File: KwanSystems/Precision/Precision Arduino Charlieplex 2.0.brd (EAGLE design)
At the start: 76.2 x 76.2 mm, 155 parts, among them J001 M04NOSILK2, J002 M04NOSILK2, J003 M06NOSILK, J201 GP-2106, J202 M06NOSILK, J405 M08NOSILK2, J406 M08NOSILK2, U201 1.8V, U202 TXB0104RUT, U401 ATMEGA328, U501 FT232RLSSOP, U602 ZF7, Y401 16MHz

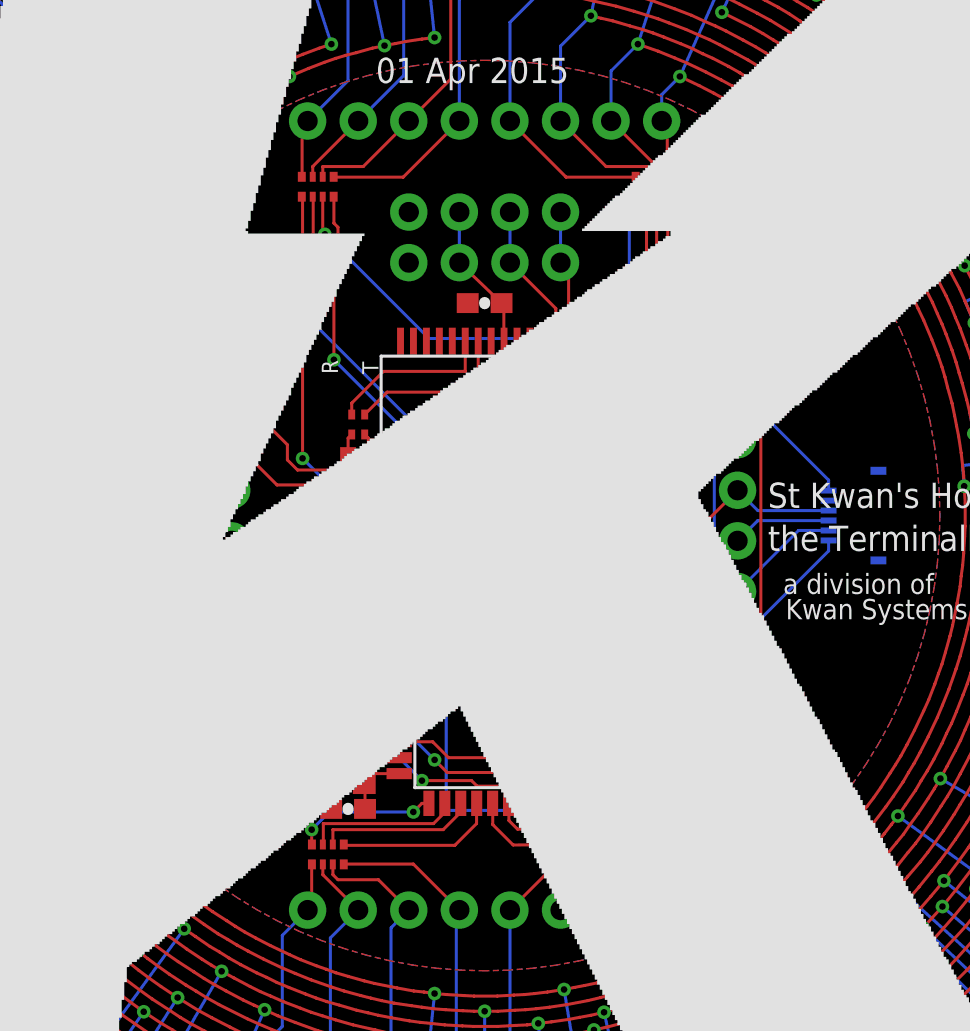
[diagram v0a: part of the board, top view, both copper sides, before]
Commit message: Added Yukari4, changed it over to use templates
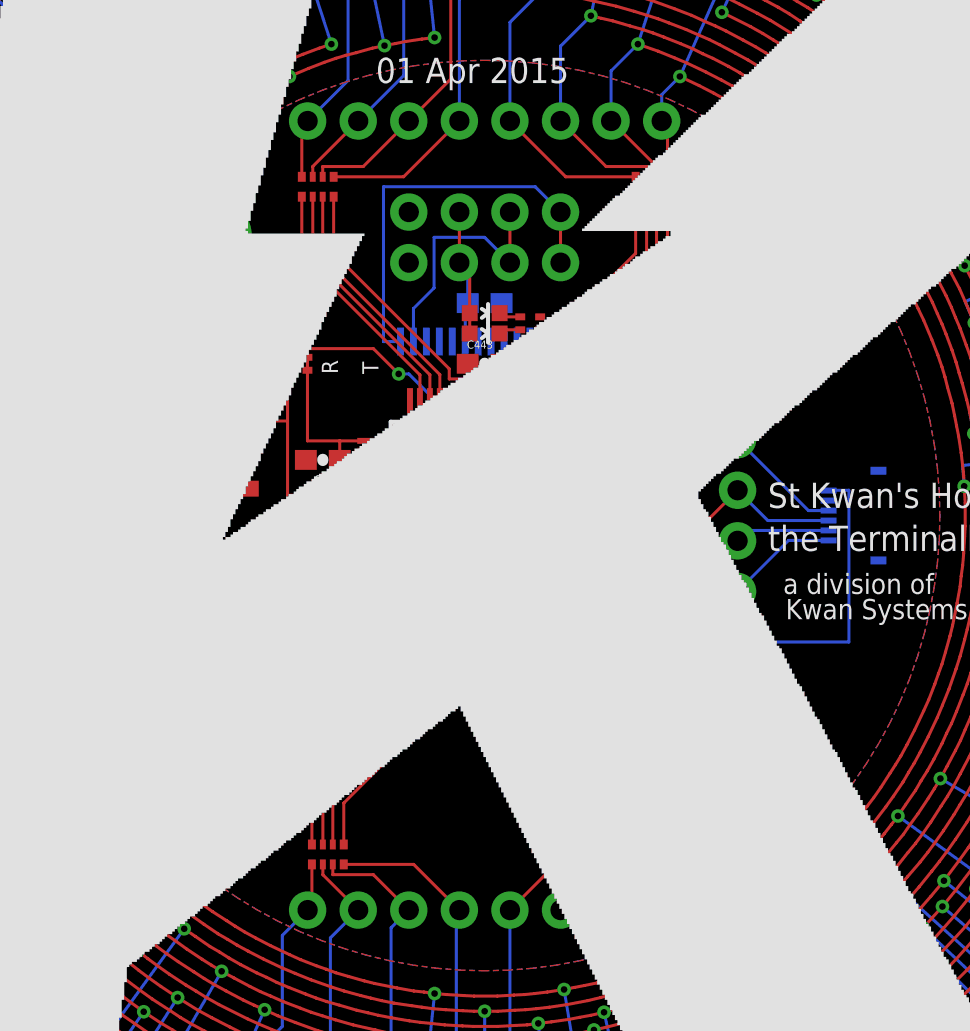
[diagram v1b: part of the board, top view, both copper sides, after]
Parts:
- removed C204: 1uF, SparkFun:0402-CAP
- removed C214: 100nF, SparkFun:0402-CAP
- removed C407, C408: 18pF, SparkFun:0603-CAP
- removed C418: 4.7uF, SparkFun:0603-CAP
- removed C420: 100nF, SparkFun:0603-CAP
- removed J003: M06NOSILK, KwanSystems:M06SIP
- removed U201: 1.8V, KwanSystems:SOT-23-5
- removed U602: ZF7, KwanSystems:SC-70-6
- removed Y401: 16MHz, KwanSystems:CRYSTAL_SMD
- added C201: 1uF, KwanSystems:CKCM25
- added C205, C423, C443, C451: 1uF, SparkFun-Capacitors:0603-CAP
- added C461: 33pF, KwanSystems:CKCM25
- added S458: B3U-1000P, KwanSystems:B3U-1000P
- added U2: AP7312, KwanSystems:SOT-23-6
- added Y1: 12MHz, KwanSystems:CRYSTAL_SMD_2MM_2_5MM
- JP1, JP2, JP3, JP4: value STAND-OFF -> STANDOFF; device SparkFun:STAND-OFF -> KwanSystems:STANDOFF
- U401: value ATMEGA328 -> LPC2148; device SparkFun:TQFP32-08 -> SparkFun:SQFP-S-10X10-64
- moved R606 16.0 mm to (28.7, 45.7), turned to 90 degrees
- moved S429 15.9 mm to (25.9, 41.1), turned to 90 degrees
- moved C215 13.0 mm to (48.0, 33.8), turned to 0 degrees
- moved D501 10.4 mm to (38.1, 48.3), turned to 270 degrees
- moved U401 10.2 mm to (38.1, 38.1)
- moved R500 10.0 mm to (40.4, 47.8), turned to 90 degrees
- moved D502 9.01 mm to (38.1, 47.2), turned to 270 degrees
- moved C502 5.86 mm to (30.0, 38.4)
- flipped C010 to the bottom
- flipped U501 to the bottom
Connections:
- removed net AREF: C420.1, U401.20
- removed net AT_RX: U401.30, U602.4
- removed net AT_TX: U202.9, U401.31, U501.5
- removed net BYP: C214.1, U201.4
- removed net RX_SEL: J003.2, R606.4, U401.16, U602.6
- removed net VCC: C010.1, C204.1, C418.2, D501.A, D502.A, J001.3, J002.3, J003.5, R606.1, R606.2, U201.1, U201.3, U202.11, U401.18, U401.4, U401.6, U501.20, U501.4, U602.5
- new net 3.3V: C201.4, C423.1, C443.1, C451.1, R606.1, R606.2, U2.1, U202.11, U401.23, U401.43, U401.49, U401.51, U401.63, U401.7
- new net 5V: C010.1, C205.1, D501.A, D502.A, J001.3, J002.3, U2.3, U2.4, U2.5, U501.20, U501.4
- new net BSL: R606.3, S458.P$1, U401.41
- new net GPS_RX: U202.9, U401.33
- new net USB_RX: U401.19, U501.5
- net 1.8V: now also C201.3, J202.6, U2.6; no longer J202.1, U201.5
- net GND: now also C201.1, C201.2, C205.2, C423.2, C443.2, C451.2, C461.1, C461.2, J202.1, JP1.P$1, JP2.P$1, JP3.P$1, JP4.P$1, S458.P$2, U2.2, U401.18, U401.25, U401.42, U401.50, U401.59, U401.6, Y1.2, Y1.4; no longer C204.2, C214.2, C407.1, C408.1, C418.1, C420.2, J003.4, J202.2, U201.2, U401.21, U401.3, U401.5, U602.2, Y401.2, Y401.4
- net GPS_TX: now also U401.34; no longer U602.3
- net LO_GPS_RX: now also J202.4; no longer J202.5
- net LO_GPS_TX: now also J202.5; no longer J202.6
- net LO_ONOFF: now also J202.3; no longer J202.4
- net LO_PPS: now also J202.2; no longer J202.3
- net P01: now also U401.17; no longer J003.1, U401.15
- net P02: now also U401.15; no longer U401.2
- net P03: now also U401.13; no longer U401.14
- net P04: now also U401.11; no longer U401.13
- net P05: now also U401.10; no longer U401.12
- net P06: now also U401.9; no longer U401.11
- net P07: now also U401.2; no longer U401.10
- net P08: now also U401.1; no longer U401.9
- net P09: now also U401.47; no longer U401.1
- net P10: now also U401.46; no longer U401.28
- net P11: now also U401.45; no longer U401.27
- net P12: now also U401.39; no longer U401.26
- net P13: now also U401.37; no longer U401.25
- net P14: now also U401.35; no longer U401.24
- net P15: now also U401.31; no longer U401.23
- net P16: now also U401.30; no longer J003.3, U401.17
- net PPS: now also U401.14; no longer U401.32
- net RESET: now also R606.4, U401.57; no longer J003.6, R606.3, U401.29
- net USB_TX: now also U401.21; no longer U602.1
- net XTAL1: now also C461.3, U401.62, Y1.3; no longer C407.2, U401.7, Y401.1
- net XTAL2: now also C461.4, U401.61, Y1.1; no longer C408.2, U401.8, Y401.3
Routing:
- net VCC: track 84.4 -> 0.00 mm, vias 5 -> 0
- net RX_SEL: track 47.7 -> 0.00 mm, vias 3 -> 0
- net P16: track 62.0 -> 16.8 mm, vias 1 -> 0
- net 3.3V: track 0.00 -> 40.0 mm
- net P11: track 43.3 -> 12.8 mm, vias 2 -> 0
- net AT_TX: track 26.7 -> 0.00 mm, vias 4 -> 0
- net RESET: track 40.6 -> 14.4 mm, vias 2 -> 0
- net BSL: track 0.00 -> 22.7 mm, vias 0 -> 2
- net PPS: track 18.3 -> 0.00 mm, vias 2 -> 0
- net 5V: track 0.00 -> 15.7 mm
- net P01: track 28.2 -> 14.0 mm, vias 1 -> 0
- net RESET_FT: track 2.12 -> 16.1 mm, vias 0 -> 1
- net USBD+: track 6.92 -> 20.6 mm
- net P13: track 26.4 -> 12.8 mm, vias 2 -> 0
- net P14: track 25.9 -> 12.6 mm, vias 2 -> 0
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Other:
- board text added: "5V"
- board text removed: "D11"
- board text removed: "D12"
- board text removed: "D13"
- board text removed: "RST"
- board text removed: "VCC"
